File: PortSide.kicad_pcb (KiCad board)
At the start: 2 copper layers, 67.5 x 59.5 mm, 32 parts, among them J1 Conn_ARM_JTAG_SWD_10, J2 USB_C_Receptacle_USB2.0_14P, J3 Conn_01x14, J4 Conn_02x08_Top_Bottom, Q1 2N7002, Q2 MMDT3904, U1 TCAN3404, U2 ESP32-S3-WROOM-1, U3 AP2112K-3.3, U4 INA226, U5 LM5164DDA, U7 CP2102N-Axx-xQFN24

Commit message: Version 2, still not happy with that
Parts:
- removed J3: Conn_01x14, Connector_PinSocket_2.54mm:PinSocket_1x14_P2.54mm_Vertical
- added J5: Conn_02x07_Counter_Clockwise, Connector_PinHeader_2.54mm:PinHeader_2x07_P2.54mm_Vertical, F.Cu at (155.5, 155.8)
- J1: footprint Connector_IDC:IDC-Header_2x05_P2.54mm_Vertical_SMD -> Connector_IDC:IDC-Header_2x05_P2.54mm_Vertical
- J2: footprint Connector_USB:USB_C_Receptacle_Amphenol_12401610E4-2A -> Connector_USB:USB_C_Receptacle_Amphenol_12401948E412A
- J4, Q1, R10, R15, U1, U7: moved to B.Cu
- Q2, R1, R13, R14, R8, R9: moved to F.Cu
- moved J2 96.6 mm to (167.8, 129.2), turned to 90 degrees
- moved R12 94.0 mm to (157.2, 137.0), turned to 180 degrees
- moved R9 92.0 mm to (156.8, 123.2)
- moved R11 91.1 mm to (157.2, 134.5), turned to 180 degrees
- moved Q2 90.5 mm to (153.5, 120.0), turned to 0 degrees
- moved R8 89.6 mm to (150.5, 123.2)
- moved R14 89.1 mm to (159.0, 131.5), turned to -90 degrees
- moved R13 85.8 mm to (159.0, 125.8), turned to 90 degrees
- moved U7 82.8 mm to (154.0, 130.0), turned to 180 degrees
- moved R10 81.3 mm to (152.8, 134.8), turned to 0 degrees
- moved J4 79.4 mm to (116.8, 159.8)
- moved U3 77.3 mm to (144.5, 143.8)
- moved U4 74.6 mm to (138.8, 143.2)
- moved R6 73.3 mm to (132.2, 137.5), turned to 180 degrees
- moved R7 73.0 mm to (132.2, 139.0), turned to 180 degrees
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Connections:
- R6 pad 1: /SCL -> /SDA
- R7 pad 1: /SDA -> /SCL
- U2 pad 15: /LCD_CS -> unconnected-(U2-IO3-Pad15)
- U2 pad 16: /LCD_RESET -> unconnected-(U2-IO46-Pad16)
- U2 pad 17: /LCD_DC -> /SCL
- U2 pad 18: /LCD_MOSI -> /SDA
- U2 pad 19: /LCD_SCK -> /INA226_ALERT
- U2 pad 20: /LCD_LED -> unconnected-(U2-IO12-Pad20)
- U2 pad 21: /LCD_MISO -> unconnected-(U2-IO13-Pad21)
- U2 pad 22: /LCD_T_CLK -> /LCD_RESET
- U2 pad 23: /LCD_T_CS -> /LCD_MOSI
- U2 pad 24: /LCD_T_DIN -> /LCD_LED
- U2 pad 25: /LCD_T_DO -> /LCD_T_CLK
- U2 pad 26: /LCD_T_IRQ -> /LCD_T_DIN
- U2 pad 28: /TCAN3404_SHDN -> /LCD_T_IRQ
- U2 pad 29: /TCAN3404_STB -> /LCD_T_DO
- U2 pad 30: /CAN_TXD -> /LCD_T_CS
- U2 pad 31: /CAN_RXD -> /LCD_MISO
- U2 pad 32: /MTMS -> /LCD_SCK
- U2 pad 33: /MTCK -> /LCD_DC
- U2 pad 34: /MTDO -> /LCD_CS
- U2 pad 35: /MTDI -> unconnected-(U2-IO42-Pad35)
- U2 pad 38: unconnected-(U2-IO2-Pad38) -> /CAN_RXD
- U2 pad 39: unconnected-(U2-IO1-Pad39) -> /CAN_TXD
- U2 pad 4: /SCL -> /MTMS
- U2 pad 5: /SDA -> /MTCK
- U2 pad 6: /INA226_ALERT -> /MTDO
- U2 pad 7: unconnected-(U2-IO7-Pad7) -> /MTDI
- U2 pad 8: unconnected-(U2-IO15-Pad8) -> /TCAN3404_SHDN
- U2 pad 9: unconnected-(U2-IO16-Pad9) -> /TCAN3404_STB
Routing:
- net GND: track 272.3 -> 45.7 mm, vias 0 -> 14
- net +3.3V: track 103.8 -> 12.0 mm, vias 4 -> 5
- net /USB_VBUS: track 35.5 -> 86.1 mm
- net /ESP_TX: track 49.7 -> 13.0 mm, vias 2 -> 1
- net /ESP_RX: track 49.2 -> 13.6 mm, vias 2 -> 1
- net /CANH: track 15.6 -> 40.1 mm
- net Net-(Q1-D): track 32.1 -> 7.79 mm, vias 2 -> 1
- net /5v_SOURCE: track 33.1 -> 10.9 mm, vias 2 -> 0
- net /ESP_IO0: track 41.9 -> 22.2 mm, vias 1 -> 2
- net /SCL: track 28.9 -> 12.6 mm
- net /LCD_CS: track 19.7 -> 35.9 mm
- net /TCAN3404_STB: track 21.7 -> 7.18 mm, vias 0 -> 1
- net /SDA: track 25.7 -> 11.6 mm
- net /LCD_T_IRQ: track 25.5 -> 12.1 mm
- net /LCD_DC: track 20.8 -> 32.8 mm
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- added copper zone on In2.Cu, net +3.3V
- added copper zone on In1.Cu, net GND
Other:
- board size 67.5 x 59.5 mm -> 58.8 x 54.2 mm
- copper layers 2 -> 4

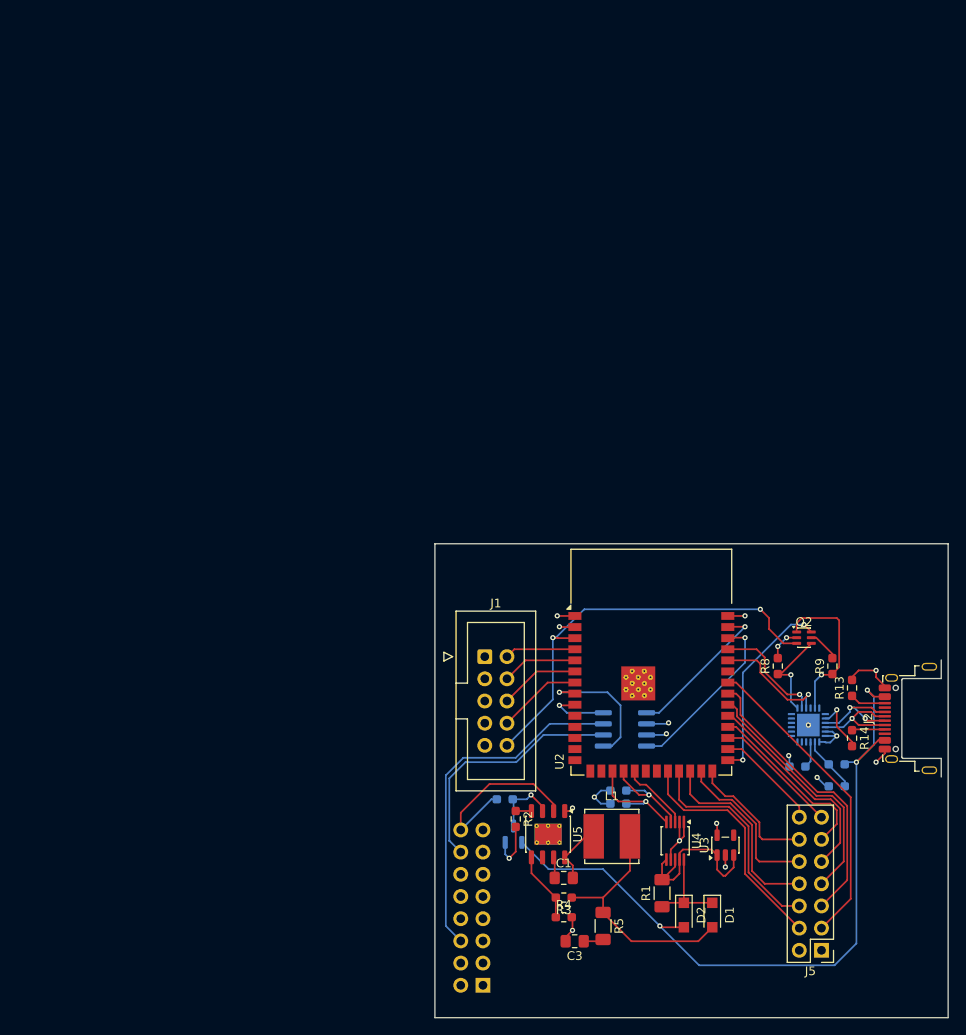
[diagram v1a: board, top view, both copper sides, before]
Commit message: Rev 3, happy. Removed INA226 and JTAG
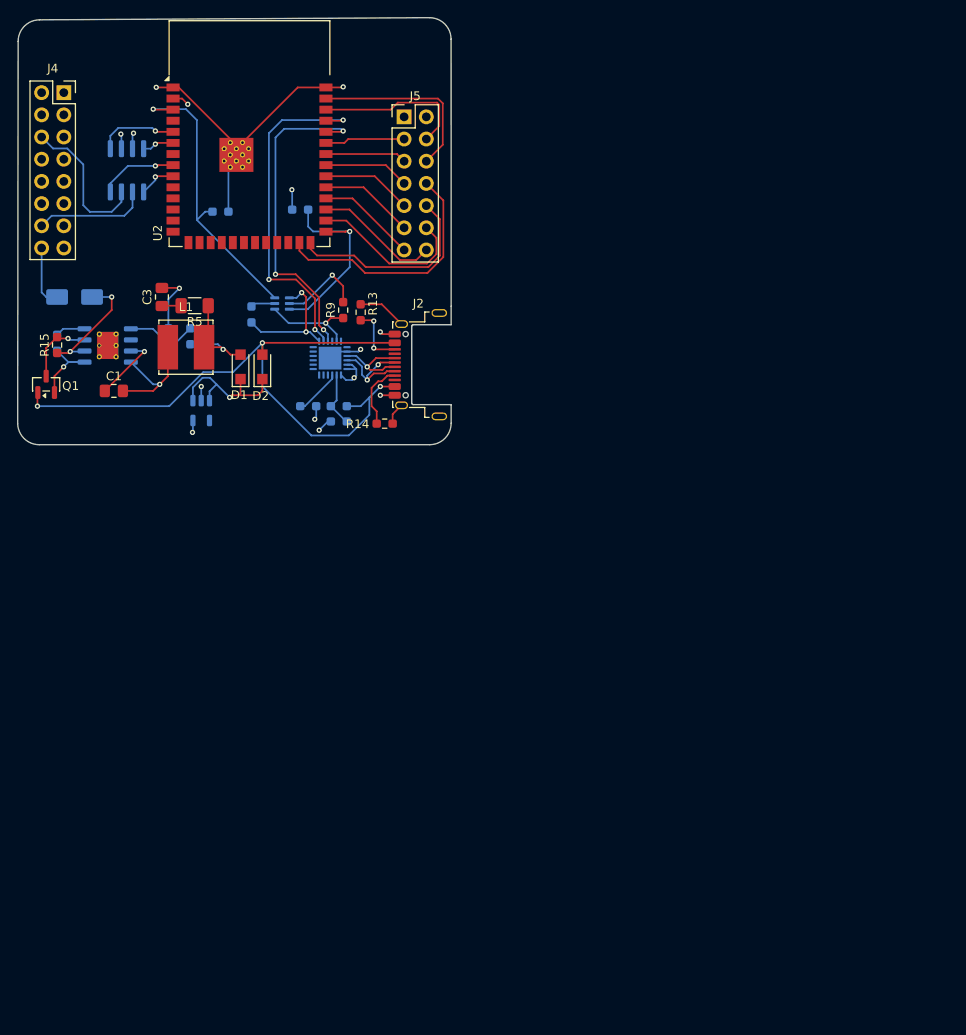
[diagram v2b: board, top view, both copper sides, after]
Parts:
- removed J1: Conn_ARM_JTAG_SWD_10, Connector_IDC:IDC-Header_2x05_P2.54mm_Vertical
- removed R1: 10m, Resistor_SMD:R_1206_3216Metric_Pad1.30x1.75mm_HandSolder
- removed R6, R7: 4.7k, Resistor_SMD:R_0603_1608Metric_Pad0.98x0.95mm_HandSolder
- removed U4: INA226, Package_SO:TSSOP-10_3x3mm_P0.5mm
- added D3: US1J, Diode_SMD:D_SMA, B.Cu at (70.0, 81.0)
- added R16: 10k, Resistor_SMD:R_0603_1608Metric_Pad0.98x0.95mm_HandSolder, B.Cu at (95.8, 71.0)
- added R17: 10k, Resistor_SMD:R_0603_1608Metric_Pad0.98x0.95mm_HandSolder, B.Cu at (86.7, 71.2)
- J4, Q1, R15: moved to F.Cu
- Q2, R2, R3, R4, R8, U3, U5: moved to B.Cu
- moved J4 112.9 mm to (68.8, 57.6)
- moved J5 106.7 mm to (107.7, 60.4), turned to 0 degrees
- moved C3 87.6 mm to (80.0, 81.0), turned to 90 degrees
- moved U1 85.7 mm to (76.0, 66.5), turned to -90 degrees
- moved R5 85.0 mm to (83.8, 82.0), turned to 180 degrees
- moved D1 82.8 mm to (89.0, 89.0), turned to 90 degrees
- moved R4 80.4 mm to (80.7, 85.5), turned to 90 degrees
- moved D2 79.2 mm to (91.5, 89.0), turned to 90 degrees
- moved U3 77.9 mm to (84.5, 94.0), turned to -90 degrees
- moved R3 77.2 mm to (83.2, 85.5), turned to 90 degrees
- moved U2 76.0 mm to (90.0, 62.3)
- moved C1 75.9 mm to (74.5, 91.8)
- moved R2 75.7 mm to (68.0, 86.2)
- moved U5 75.3 mm to (73.8, 86.5), turned to 0 degrees
- moved Q1 74.3 mm to (66.8, 91.0)
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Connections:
- J4 pad 16: /CAR_POS -> Net-(D3-A)
- U2 pad 17: /SCL -> unconnected-(U2-IO9-Pad17)
- U2 pad 18: /SDA -> unconnected-(U2-IO10-Pad18)
- U2 pad 19: /INA226_ALERT -> unconnected-(U2-IO11-Pad19)
- U2 pad 22: /LCD_RESET -> unconnected-(U2-IO14-Pad22)
- U2 pad 23: /LCD_MOSI -> unconnected-(U2-IO21-Pad23)
- U2 pad 24: /LCD_LED -> unconnected-(U2-IO47-Pad24)
- U2 pad 25: /LCD_T_CLK -> /LCD_LED
- U2 pad 26: /LCD_T_DIN -> /LCD_T_CLK
- U2 pad 28: /LCD_T_IRQ -> /LCD_T_DIN
- U2 pad 29: /LCD_T_DO -> /LCD_T_IRQ
- U2 pad 30: /LCD_T_CS -> /LCD_T_DO
- U2 pad 31: /LCD_MISO -> /LCD_T_CS
- U2 pad 32: /LCD_SCK -> /LCD_MISO
- U2 pad 33: /LCD_DC -> /LCD_SCK
- U2 pad 34: /LCD_CS -> /LCD_DC
- U2 pad 35: unconnected-(U2-IO42-Pad35) -> /LCD_CS
- U2 pad 38: /CAN_RXD -> /LCD_RESET
- U2 pad 39: /CAN_TXD -> /LCD_MOSI
- U2 pad 4: /MTMS -> unconnected-(U2-IO4-Pad4)
- U2 pad 5: /MTCK -> /CAN_TXD
- U2 pad 6: /MTDO -> /CAN_RXD
- U2 pad 7: /MTDI -> unconnected-(U2-IO7-Pad7)
- U2 pad 8: /TCAN3404_SHDN -> /TCAN3404_STB
- U2 pad 9: /TCAN3404_STB -> /TCAN3404_SHDN
- U3 pad 1: +5V -> /5v_SOURCE
- U3 pad 3: +5V -> /5v_SOURCE
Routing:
- net /LCD_CS: track 35.9 -> 9.13 mm
- net /ESP_TX: track 13.0 -> 39.4 mm, vias 1 -> 3
- net GND: track 45.7 -> 70.3 mm, vias 14 -> 11
- net /ESP_RX: track 13.6 -> 37.4 mm, vias 1 -> 3
- net /LCD_DC: track 32.8 -> 9.29 mm
- net /CANH: track 40.1 -> 17.0 mm
- net +5V: track 20.5 -> 0.00 mm
- net /LCD_SCK: track 28.4 -> 9.82 mm
- net /CAN_RXD: track 20.1 -> 3.64 mm
- net /CANL: track 28.7 -> 13.1 mm
- net /5V_BUCK: track 28.1 -> 13.5 mm, vias 0 -> 1
- net /ESP_EN: track 48.7 -> 34.0 mm, vias 2 -> 1
- net /LCD_MISO: track 24.2 -> 10.3 mm
- net /SCL: track 12.6 -> 0.00 mm, vias 1 -> 0
- net /SDA: track 11.6 -> 0.00 mm, vias 1 -> 0
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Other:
- board size 58.8 x 54.2 mm -> 49.6 x 48.9 mm
